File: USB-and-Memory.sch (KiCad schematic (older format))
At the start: 0 parts

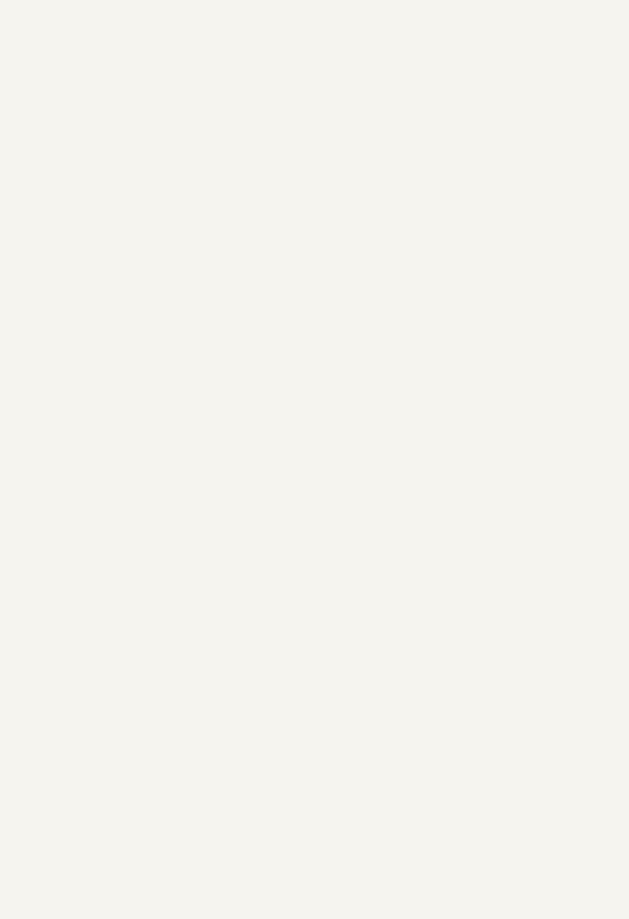
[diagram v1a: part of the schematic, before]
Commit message: Continued work on schematic and board planning
Signed-off-by: Eldalote <Eldalote.Electronics@gmail.com>
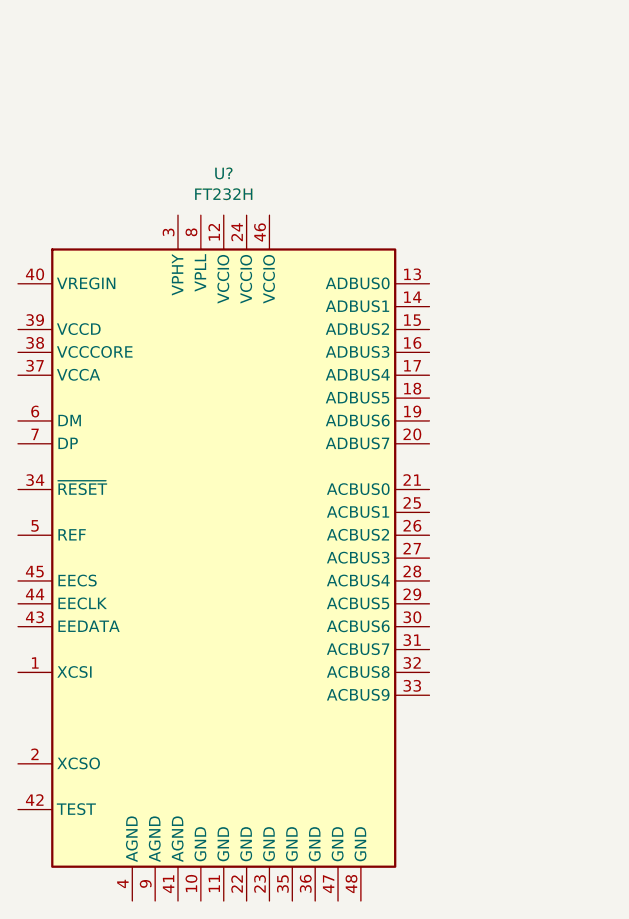
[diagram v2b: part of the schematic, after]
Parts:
- added U?: FT232H, Package_QFP:LQFP-48_7x7mm_P0.5mm, symbol Interface_USB:FT232H
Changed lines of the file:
@@
 Text Notes 4800 1600 0    59   ~ 0
 USB: FTDI FT232H or FTDI FT232R\n\nMemory: Memory for FPGA bitstream data: MT25QL128ABA (non-JLC part)\n\nMemory: For FPGA user accessable data storage: W25Q128JVSIQ \n
+$Comp
+L Interface_USB:FT232H U?
+U 1 1 5F5894AD
+P 3000 3800
+F 0 "U?" H 3000 5481 50  0000 C CNN
+F 1 "FT232H" H 3000 5390 50  0000 C CNN
+F 2 "Package_QFP:LQFP-48_7x7mm_P0.5mm" H 3000 3800 50  0001 C CNN
+F 3 "https://www.ftdichip.com/Support/Documents/DataSheets/ICs/DS_FT232H.pdf" H 3000 3800 50  0001 C CNN
+F 4 "895-FT232HL-REEL" H 3000 3800 50  0001 C CNN "Mouser"
+F 5 "768-1101-1-ND " H 3000 3800 50  0001 C CNN "DigiKey"
+F 6 "Extended and expensive" H 3000 3800 50  0001 C CNN "LCSC"
+	1    3000 3800
+	1    0    0    -1
+$EndComp
 $EndSCHEMATC

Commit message: More of the same
Signed-off-by: Eldalote <Eldalote.Electronics@gmail.com>
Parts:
- gave numbers to parts that had none: 1
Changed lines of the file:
@@
 USB: FTDI FT232H or FTDI FT232R\n\nMemory: Memory for FPGA bitstream data: MT25QL128ABA (non-JLC part)\n\nMemory: For FPGA user accessable data storage: W25Q128JVSIQ \n
 $Comp
-L Interface_USB:FT232H U?
+L Interface_USB:FT232H U301
 U 1 1 5F5894AD
 P 3000 3800
-F 0 "U?" H 3000 5481 50  0000 C CNN
+F 0 "U301" H 3000 5481 50  0000 C CNN
 F 1 "FT232H" H 3000 5390 50  0000 C CNN
 F 2 "Package_QFP:LQFP-48_7x7mm_P0.5mm" H 3000 3800 50  0001 C CNN

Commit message: Further work
Signed-off-by: Eldalote <Eldalote.Electronics@gmail.com>
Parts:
- added J301: UJ2-MBH-1-SMT-TR, digikey-footprints:USB_Mini_B_Female_UJ2-MBH-1-SMT-TR, symbol dk_USB-DVI-HDMI-Connectors:UJ2-MBH-1-SMT-TR
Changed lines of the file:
@@
 $Descr A4 11693 8268
 encoding utf-8
-Sheet 3 11
+Sheet 3 12
 Title ""
 Date ""
@@
 	1    0    0    -1
 $EndComp
+$Comp
+L dk_USB-DVI-HDMI-Connectors:UJ2-MBH-1-SMT-TR J301
+U 1 1 5F5BD744
+P 5100 6000
+F 0 "J301" H 5125 6652 60  0000 C CNN
+F 1 "UJ2-MBH-1-SMT-TR" H 5125 6546 60  0000 C CNN
+F 2 "digikey-footprints:USB_Mini_B_Female_UJ2-MBH-1-SMT-TR" H 5300 6200 60  0001 L CNN
+F 3 "https://www.cui.com/product/resource/digikeypdf/uj2-mbh-smt.pdf" H 5300 6300 60  0001 L CNN
+F 4 "102-4003-1-ND" H 5300 6400 60  0001 L CNN "Digi-Key_PN"
+F 5 "UJ2-MBH-1-SMT-TR" H 5300 6500 60  0001 L CNN "MPN"
+F 6 "Connectors, Interconnects" H 5300 6600 60  0001 L CNN "Category"
+F 7 "USB, DVI, HDMI Connectors" H 5300 6700 60  0001 L CNN "Family"
+F 8 "https://www.cui.com/product/resource/digikeypdf/uj2-mbh-smt.pdf" H 5300 6800 60  0001 L CNN "DK_Datasheet_Link"
+F 9 "/product-detail/en/cui-inc/UJ2-MBH-1-SMT-TR/102-4003-1-ND/6187925" H 5300 6900 60  0001 L CNN "DK_Detail_Page"
+F 10 "CONN RCPT USB2.0 MINI B SMD R/A" H 5300 7000 60  0001 L CNN "Description"
+F 11 "CUI Inc." H 5300 7100 60  0001 L CNN "Manufacturer"
+F 12 "Active" H 5300 7200 60  0001 L CNN "Status"
+	1    5100 6000
+	1    0    0    -1
+$EndComp

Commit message: Made progress woth power
Signed-off-by: Jan Mart Liewes <Eldalote.Electronics@gmail.com>
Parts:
- renumbered J301 to J601, U301 to U601
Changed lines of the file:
@@
 $Descr A4 11693 8268
 encoding utf-8
-Sheet 3 12
+Sheet 4 15
 Title ""
 Date ""
@@
 USB: FTDI FT232H or FTDI FT232R\n\nMemory: Memory for FPGA bitstream data: MT25QL128ABA (non-JLC part)\n\nMemory: For FPGA user accessable data storage: W25Q128JVSIQ \n
 $Comp
-L Interface_USB:FT232H U301
+L Interface_USB:FT232H U601
 U 1 1 5F5894AD
 P 3000 3800
-F 0 "U301" H 3000 5481 50  0000 C CNN
+F 0 "U601" H 3000 5481 50  0000 C CNN
 F 1 "FT232H" H 3000 5390 50  0000 C CNN
 F 2 "Package_QFP:LQFP-48_7x7mm_P0.5mm" H 3000 3800 50  0001 C CNN
@@
 $EndComp
 $Comp
-L dk_USB-DVI-HDMI-Connectors:UJ2-MBH-1-SMT-TR J301
+L dk_USB-DVI-HDMI-Connectors:UJ2-MBH-1-SMT-TR J601
 U 1 1 5F5BD744
 P 5100 6000
-F 0 "J301" H 5125 6652 60  0000 C CNN
+F 0 "J601" H 5125 6652 60  0000 C CNN
 F 1 "UJ2-MBH-1-SMT-TR" H 5125 6546 60  0000 C CNN
 F 2 "digikey-footprints:USB_Mini_B_Female_UJ2-MBH-1-SMT-TR" H 5300 6200 60  0001 L CNN
